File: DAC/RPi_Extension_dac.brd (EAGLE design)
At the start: 63 x 50 mm, 41 parts, among them U1 AD5360BSTZ, U2 ADR423ARZ

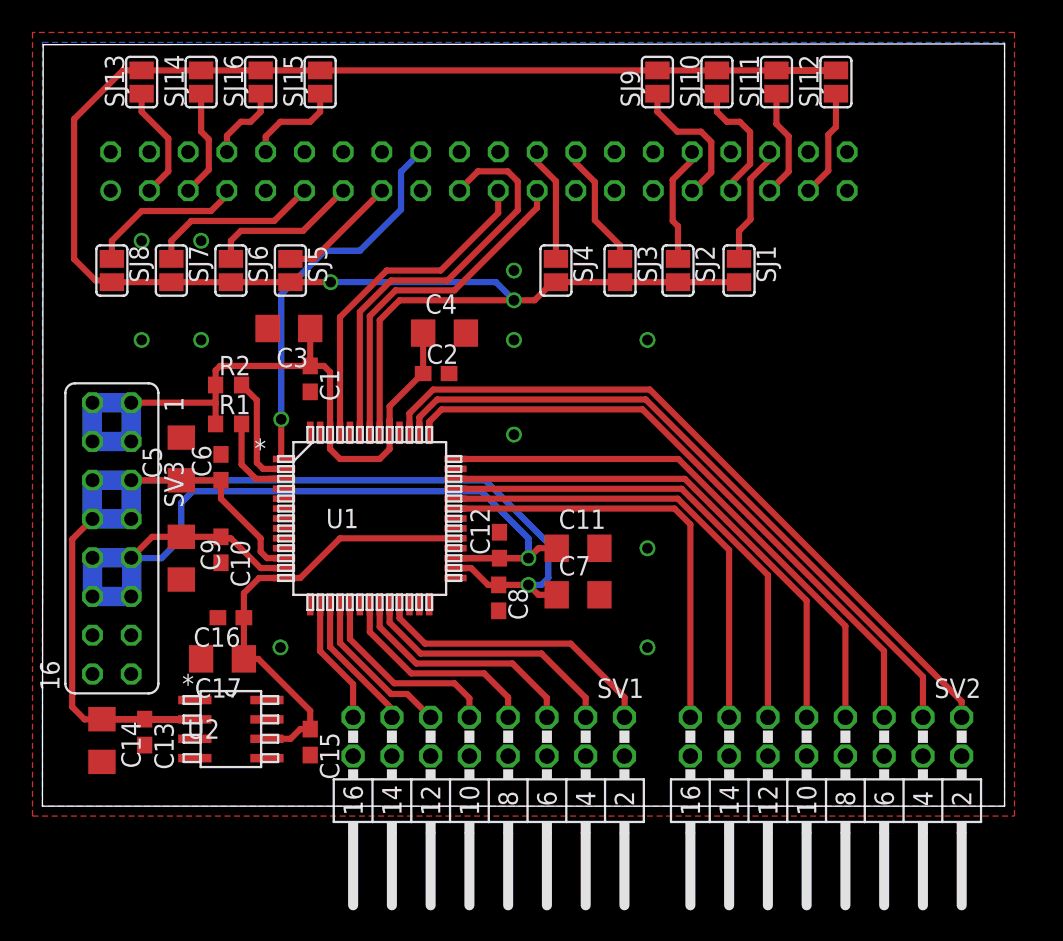
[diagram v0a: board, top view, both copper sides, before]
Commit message: cleaned up silklayer of dac board
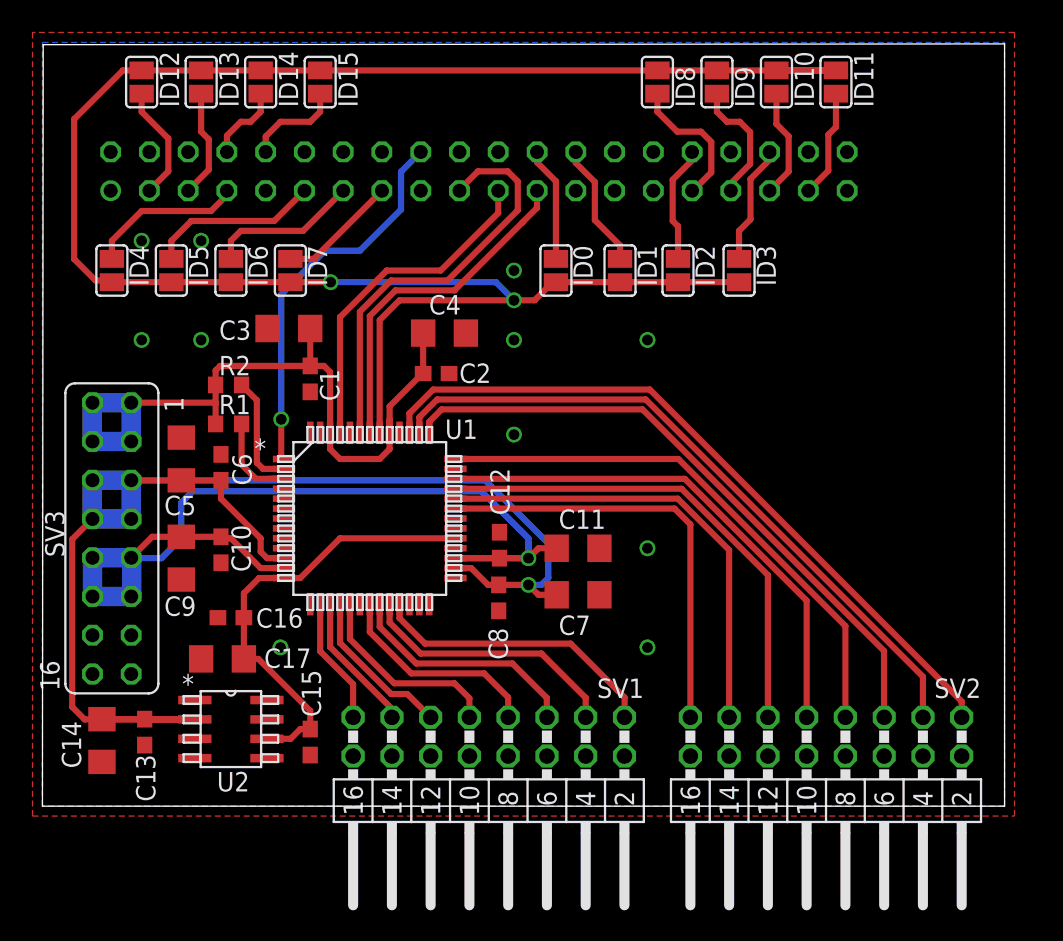
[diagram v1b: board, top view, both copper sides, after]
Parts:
- renumbered SJ1 to ID3, SJ10 to ID9, SJ11 to ID10, SJ12 to ID11, SJ13 to ID12, SJ14 to ID13, SJ15 to ID15, SJ16 to ID14, SJ2 to ID2, SJ3 to ID1, SJ4 to ID0, SJ5 to ID7, SJ6 to ID6, SJ7 to ID5, SJ8 to ID4, SJ9 to ID8, SV5 to SV4
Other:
- board text added: "Hitzmann 2017"

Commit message: updated content before making repository public
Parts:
- added S1: (no value), switch-omron:B3F-10XX
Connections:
- net GND: now also S1.1, S1.2
- net N$18: now also S1.4
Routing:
- net N$18: track 6.82 -> 59.2 mm, vias 0 -> 1
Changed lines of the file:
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@@
 <?xml version="1.0" encoding="utf-8"?>
 <!DOCTYPE eagle SYSTEM "eagle.dtd">
-<eagle version="7.6.0">
+<eagle version="8.1.0">
 <drawing>
 <settings>
@@
 </element>
 <element name="SV1" library="con-lstb" package="MA08-2W" value="" x="29.25" y="4.55" rot="R180">
+<attribute name="MF" value="" x="29.25" y="4.55" size="1.778" layer="27" rot="R180" display="off"/>
 <attribute name="MPN" value="" x="29.25" y="4.55" size="1.778" layer="27" rot="R180" display="off"/>
-<attribute name="MF" value="" x="29.25" y="4.55" size="1.778" layer="27" rot="R180" display="off"/>
+<attribute name="OC_FARNELL" value="unknown" x="29.25" y="4.55" size="1.778" layer="27" rot="R180" display="off"/>
 <attribute name="OC_NEWARK" value="unknown" x="29.25" y="4.55" size="1.778" layer="27" rot="R180" display="off"/>
-<attribute name="OC_FARNELL" value="unknown" x="29.25" y="4.55" size="1.778" layer="27" rot="R180" display="off"/>
 </element>
 <element name="C1" library="rcl" package="C0603" value="100nF" x="17.55" y="28" rot="R270"/>
@@
 </element>
 <element name="SV3" library="con-lsta" package="FE08-2" value="" x="4.55" y="17.55" smashed="yes" rot="R270">
+<attribute name="MF" value="" x="4.55" y="17.55" size="1.778" layer="27" rot="R270" display="off"/>
 <attribute name="MPN" value="" x="4.55" y="17.55" size="1.778" layer="27" rot="R270" display="off"/>
-<attribute name="MF" value="" x="4.55" y="17.55" size="1.778" layer="27" rot="R270" display="off"/>
+<attribute name="NAME" x="0.179" y="19.38" size="1.27" layer="25" ratio="10" rot="R270"/>
+<attribute name="OC_FARNELL" value="unknown" x="4.55" y="17.55" size="1.778" layer="27" rot="R270" display="off"/>
 <attribute name="OC_NEWARK" value="unknown" x="4.55" y="17.55" size="1.778" layer="27" rot="R270" display="off"/>
-<attribute name="OC_FARNELL" value="unknown" x="4.55" y="17.55" size="1.778" layer="27" rot="R270" display="off"/>
-<attribute name="NAME" x="0.179" y="19.38" size="1.27" layer="25" ratio="10" rot="R270"/>
 <attribute name="VALUE" x="-0.149" y="27.71" size="1.27" layer="27" ratio="10" rot="R270"/>
 </element>
@@
 <element name="U2" library="ADR423ARZ" package="R_8" value="ADR423ARZ" x="12.35" y="5.05" smashed="yes">
 <attribute name="MANUFACTURER_PART_NUMBER" value="ADR423ARZ" x="12.35" y="5.05" size="1.778" layer="27" display="off"/>
-<attribute name="VENDOR" value="Vendor" x="12.35" y="5.05" size="1.778" layer="27" display="off"/>
 <attribute name="NAME" x="11.4298" y="0.965" size="1.27" layer="25" ratio="6" rot="SR0"/>
 <attribute name="VALUE" x="9.0734" y="4.415" size="1.27" layer="27" ratio="6" rot="SR0"/>
+<attribute name="VENDOR" value="Vendor" x="12.35" y="5.05" size="1.778" layer="27" display="off"/>
 </element>
 <element name="C13" library="rcl" package="C0603" value="100nF" x="6.7" y="4.85" smashed="yes" rot="R270">
@@
 <attribute name="MF" value="" x="28.6" y="41.6" size="1.778" layer="28" rot="MR180" display="off"/>
 <attribute name="MPN" value="" x="28.6" y="41.6" size="1.778" layer="28" rot="MR180" display="off"/>
+<attribute name="NAME" x="27.13" y="46.621" size="1.27" layer="26" ratio="10" rot="MR180"/>
 <attribute name="OC_FARNELL" value="unknown" x="28.6" y="41.6" size="1.778" layer="28" rot="MR180" display="off"/>
 <attribute name="OC_NEWARK" value="unknown" x="28.6" y="41.6" size="1.778" layer="28" rot="MR180" display="off"/>
-<attribute name="NAME" x="27.13" y="46.621" size="1.27" layer="26" ratio="10" rot="MR180"/>
 <attribute name="VALUE" x="3.2" y="46.299" size="1.27" layer="28" ratio="10" rot="MR180"/>
 </element>
@@
 <attribute name="NAME" x="16.757" y="45.799" size="1.27" layer="25" ratio="10" rot="R90"/>
 <attribute name="VALUE" x="14.3" y="47.8501" size="0.02" layer="27" rot="R90"/>
+</element>
+<element name="S1" library="switch-omron" package="B3F-10XX" value="" x="59.15" y="32.5" rot="R270">
+<attribute name="MF" value="" x="59.15" y="32.5" size="1.778" layer="27" rot="R270" display="off"/>
+<attribute name="MPN" value="B3F-1000" x="59.15" y="32.5" size="1.778" layer="27" rot="R270" display="off"/>
+<attribute name="OC_FARNELL" value="176432" x="59.15" y="32.5" size="1.778" layer="27" rot="R270" display="off"/>
+<attribute name="OC_NEWARK" value="36M3542" x="59.15" y="32.5" size="1.778" layer="27" rot="R270" display="off"/>
 </element>
 </elements>
@@
 <contactref element="SV4" pad="14"/>
 <contactref element="SV4" pad="39"/>
+<contactref element="S1" pad="1"/>
+<contactref element="S1" pad="2"/>
 </signal>
 <signal name="DVCC">
@@
 <wire x1="13.05" y1="22.3894125" x2="13.9894125" y2="21.45" width="0.4064" layer="1"/>
 <wire x1="13.9894125" y1="21.45" x2="15.8366" y2="21.45" width="0.4064" layer="1"/>
+<contactref element="S1" pad="4"/>
+<wire x1="56.8894" y1="29.2488" x2="53.9488" y2="29.2488" width="0.4064" layer="16"/>
+<wire x1="53.9488" y1="29.2488" x2="36.4" y2="11.7" width="0.4064" layer="16"/>
+<wire x1="27.3" y1="11.7" x2="36.4" y2="11.7" width="0.4064" layer="16"/>
+<wire x1="15.8366" y1="21.45" x2="17.55" y2="21.45" width="0.4064" layer="1"/>
+<wire x1="17.55" y1="21.45" x2="19.5" y2="19.5" width="0.4064" layer="1"/>
+<via x="19.5" y="19.5" extent="1-16" drill="0.7"/>
+<wire x1="19.5" y1="19.5" x2="27.3" y2="11.7" width="0.4064" layer="16"/>
 </signal>
 <signal name="LDAC">

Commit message: updated reference voltage on dac board
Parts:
- U2: value ADR423ARZ -> ADR425ARZ
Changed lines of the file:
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@@
 <?xml version="1.0" encoding="utf-8"?>
 <!DOCTYPE eagle SYSTEM "eagle.dtd">
-<eagle version="8.1.0">
+<eagle version="8.4.3">
 <drawing>
 <settings>
 <setting alwaysvectorfont="no"/>
+<setting keepoldvectorfont="yes"/>
 <setting verticaltext="up"/>
 </settings>
@@
 <param name="dpMaxLengthDifference" value="10mm"/>
 <param name="dpGapFactor" value="2.5"/>
-<param name="checkGrid" value="0"/>
 <param name="checkAngle" value="0"/>
 <param name="checkFont" value="1"/>
 <param name="checkRestrict" value="1"/>
+<param name="checkStop" value="0"/>
 <param name="useDiameter" value="13"/>
 <param name="maxErrors" value="50"/>
@@
 <element name="ID1" library="jumper" package="SJ" value="" x="37.85" y="35.1" rot="R270"/>
 <element name="ID0" library="jumper" package="SJ" value="" x="33.65" y="35.1" rot="R270"/>
-<element name="U2" library="ADR423ARZ" package="R_8" value="ADR423ARZ" x="12.35" y="5.05" smashed="yes">
+<element name="U2" library="ADR423ARZ" package="R_8" value="ADR425ARZ" x="12.35" y="5.05" smashed="yes">
 <attribute name="MANUFACTURER_PART_NUMBER" value="ADR423ARZ" x="12.35" y="5.05" size="1.778" layer="27" display="off"/>
 <attribute name="NAME" x="11.4298" y="0.965" size="1.27" layer="25" ratio="6" rot="SR0"/>
